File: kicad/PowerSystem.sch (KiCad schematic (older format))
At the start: 0 parts

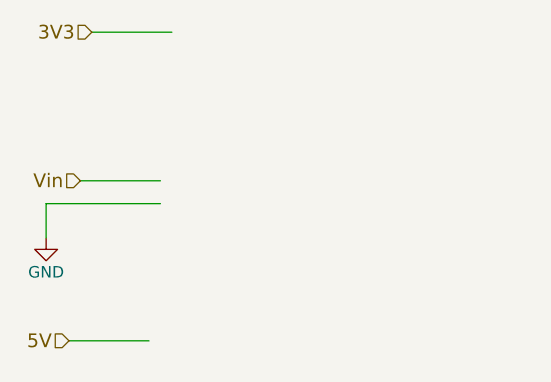
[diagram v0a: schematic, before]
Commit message: Completed the new schematic (draft) and started the layout to verify the design
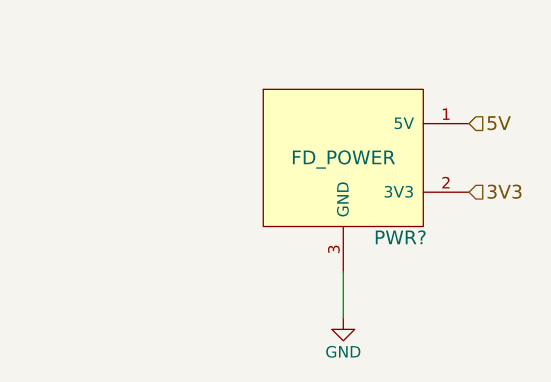
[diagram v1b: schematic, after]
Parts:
- added PWR?: FD_POWER, symbol FD_POWER
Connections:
- net labels removed: Vin
- wire segments 5 -> 1
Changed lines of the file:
@@
 Comment4 ""
 $EndDescr
-Text HLabel 2750 1950 0    60   Input ~ 0
+Text HLabel 4400 2650 2    60   Input ~ 0
 3V3
-Text HLabel 2700 2600 0    60   Input ~ 0
-Vin
-Text HLabel 2650 3300 0    60   Input ~ 0
+Text HLabel 4400 2350 2    60   Input ~ 0
 5V
 $Comp
-L GND #PWR?
-U 1 1 5A715D47
-P 2550 2850
-F 0 "#PWR?" H 2550 2600 50  0001 C CNN
-F 1 "GND" H 2550 2700 50  0000 C CNN
-F 2 "" H 2550 2850 50  0001 C CNN
-F 3 "" H 2550 2850 50  0001 C CNN
-	1    2550 2850
+L FD_POWER PWR?
+U 1 1 5A738B85
+P 3500 2700
+F 0 "PWR?" H 4100 2550 60  0000 C CNN
+F 1 "FD_POWER" H 3850 2900 60  0000 C CNN
+F 2 "" H 3500 2700 60  0001 C CNN
+F 3 "" H 3500 2700 60  0001 C CNN
+	1    3500 2700
 	1    0    0    -1
 $EndComp
 Wire Wire Line
-	2550 2850 2550 2700
-Wire Wire Line
-	2550 2700 3050 2700
-Wire Wire Line
-	2700 2600 3050 2600
-Wire Wire Line
-	2650 3300 3000 3300
-Wire Wire Line
-	2750 1950 3100 1950
+	3850 3000 3850 3200
+$Comp
+L GND #PWR?
+U 1 1 5A738BC6
+P 3850 3200
+F 0 "#PWR?" H 3850 2950 50  0001 C CNN
+F 1 "GND" H 3850 3050 50  0000 C CNN
+F 2 "" H 3850 3200 50  0001 C CNN
+F 3 "" H 3850 3200 50  0001 C CNN
+	1    3850 3200
+	1    0    0    -1
+$EndComp
 $EndSCHEMATC
